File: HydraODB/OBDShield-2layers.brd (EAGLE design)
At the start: 59.9 x 37 mm, 24 parts, among them IC1 LM317MABDT, J1 HYDRABUS_SHIELD_CON_HEADER_2X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, J2 HYDRABUS_SHIELD_CON_HEADER_2X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, J3 HYDRABUS_SHIELD_CON_HEADER_2X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, U1 SN65HVD233DG4, U2 SN65HVD233DG4

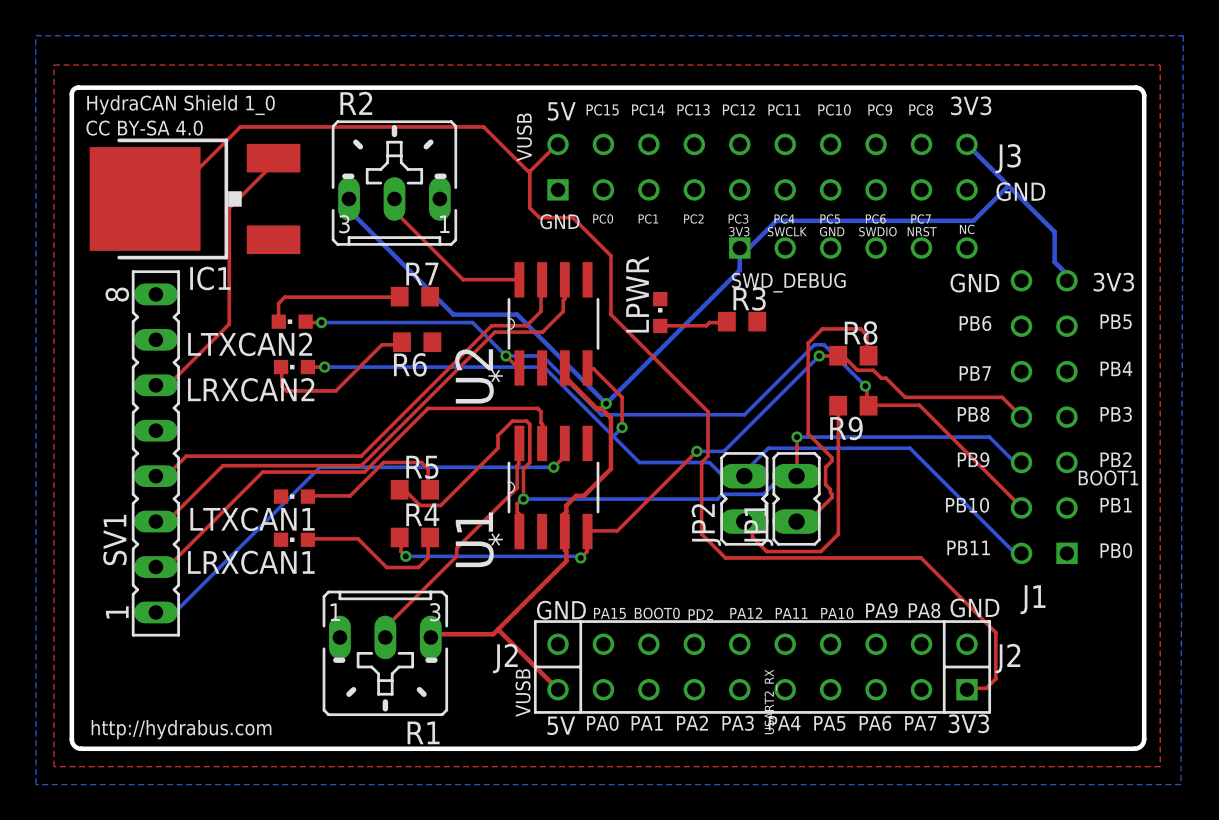
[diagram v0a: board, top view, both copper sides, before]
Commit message: Corrected J2 mirror
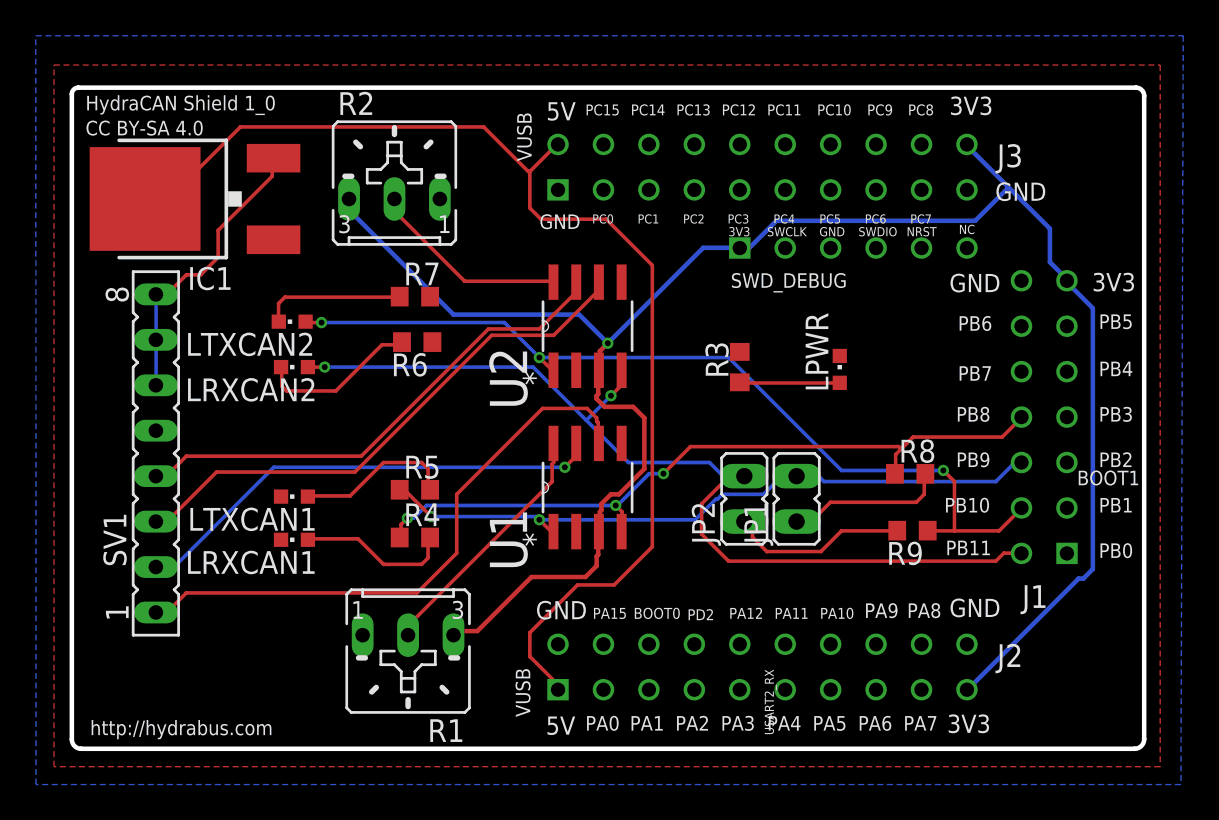
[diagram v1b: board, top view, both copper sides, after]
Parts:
- moved LPWR 10.5 mm to (42.9, 21.2)
- moved R9 7.73 mm to (47.0, 12.2)
- moved R8 7.33 mm to (46.9, 15.4)
- moved R3 2.54 mm to (37.3, 21.3), turned to 90 degrees
- moved U2 1.91 mm to (28.8, 23.6)
- moved U1 1.91 mm to (28.8, 14.6)
- moved R1 1.28 mm to (18.8, 5.46)
- flipped J2 to the top
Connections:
- net +12V: now also SV1.7, SV1.8
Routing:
- net +3V3: track 85.6 -> 106.6 mm
- net VUSB: track 75.2 -> 65.0 mm
- net PB10: track 47.7 -> 38.1 mm
- net N$19: track 17.0 -> 8.93 mm
- net N$9: track 27.2 -> 33.0 mm, vias 1 -> 0
- net N$16: track 13.8 -> 9.97 mm
- net PB9: track 50.7 -> 54.0 mm
- net N$17: track 9.24 -> 11.2 mm
- net N$14: track 3.82 -> 5.63 mm
- net N$12: track 27.1 -> 28.3 mm
- net PB8: track 42.4 -> 41.3 mm, vias 4 -> 3
- net N$11: track 29.4 -> 30.6 mm
- net N$10: track 27.1 -> 26.8 mm, vias 0 -> 1
